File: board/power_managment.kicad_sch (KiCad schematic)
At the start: 26 parts, among them J3 Bat IN Terminal, J4 Bat OUT Terminal, Q1 PMOS, U1 INA226, U3 AMS1117-3.3, U3 INA226, U4 LM2596S-5

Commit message: More work on PCB design
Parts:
- removed C5: 100n, Capacitor_SMD:C_0201_0603Metric, symbol Device:C
- C1: footprint Diode_THT:D_DO-201_P12.70mm_Horizontal -> Capacitor_SMD:C_0603_1608Metric
- C15: footprint Capacitor_SMD:C_0603_1608Metric -> Capacitor_THT:CP_Radial_D8.0mm_P3.50mm
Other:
- moved on the sheet: C15, F1
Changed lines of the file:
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@@
     (rev "1.0")
   )
-  (junction (at 145.415 66.675) (diameter 0) (color 0 0 0 0)
-  )
   (junction (at 112.395 66.675) (diameter 0) (color 0 0 0 0)
   )
@@
   )
   (junction (at 138.43 125.095) (diameter 0) (color 0 0 0 0)
-  )
-  (junction (at 156.21 66.675) (diameter 0) (color 0 0 0 0)
   )
   (junction (at 271.145 114.935) (diameter 0) (color 0 0 0 0)
@@
     (stroke (width 0) (type default))
   )
-  (wire (pts (xy 141.605 66.675) (xy 145.415 66.675))
-    (stroke (width 0) (type default))
-  )
   (wire (pts (xy 254.635 114.935) (xy 268.605 114.935))
     (stroke (width 0) (type default))
@@
     (stroke (width 0) (type default))
   )
+  (wire (pts (xy 141.605 66.675) (xy 141.605 78.74))
+    (stroke (width 0) (type default))
+  )
   (wire (pts (xy 33.655 154.305) (xy 51.435 154.305))
     (stroke (width 0) (type default))
   )
-  (wire (pts (xy 156.21 66.675) (xy 161.925 66.675))
+  (wire (pts (xy 128.905 66.675) (xy 141.605 66.675))
     (stroke (width 0) (type default))
   )
@@
     (stroke (width 0) (type default))
   )
-  (wire (pts (xy 145.415 66.675) (xy 156.21 66.675))
-    (stroke (width 0) (type default))
-  )
   (wire (pts (xy 254.635 55.245) (xy 268.605 55.245))
     (stroke (width 0) (type default))
@@
     (stroke (width 0) (type default))
   )
-  (wire (pts (xy 145.415 66.675) (xy 145.415 78.105))
-    (stroke (width 0) (type default))
-  )
   (wire (pts (xy 271.145 100.33) (xy 271.145 104.775))
     (stroke (width 0) (type default))
   )
+  (wire (pts (xy 141.605 66.675) (xy 155.575 66.675))
+    (stroke (width 0) (type default))
+  )
   (wire (pts (xy 254.635 42.545) (xy 268.605 42.545))
     (stroke (width 0) (type default))
@@
     (stroke (width 0) (type default))
   )
-  (wire (pts (xy 156.21 85.725) (xy 156.21 97.79))
+  (wire (pts (xy 141.605 86.36) (xy 141.605 98.425))
     (stroke (width 0) (type default))
   )
@@
     (stroke (width 0) (type default))
   )
-  (wire (pts (xy 156.21 97.79) (xy 154.94 97.79))
-    (stroke (width 0) (type default))
-  )
   (wire (pts (xy 268.605 102.235) (xy 268.605 114.935))
     (stroke (width 0) (type default))
@@
     (stroke (width 0) (type default))
   )
-  (wire (pts (xy 128.905 66.675) (xy 141.605 66.675))
-    (stroke (width 0) (type default))
-  )
   (wire (pts (xy 61.595 128.905) (xy 61.595 136.525))
     (stroke (width 0) (type default))
@@
     (stroke (width 0) (type default))
   )
-  (wire (pts (xy 169.545 66.675) (xy 177.8 66.675))
+  (wire (pts (xy 163.195 66.675) (xy 171.45 66.675))
     (stroke (width 0) (type default))
   )
@@
     (stroke (width 0) (type default))
   )
-  (wire (pts (xy 156.21 66.675) (xy 156.21 78.105))
-    (stroke (width 0) (type default))
-  )
   (wire (pts (xy 29.845 129.54) (xy 29.845 128.905))
     (stroke (width 0) (type default))
@@
   )
   (wire (pts (xy 268.605 114.935) (xy 271.145 114.935))
-    (stroke (width 0) (type default))
-  )
-  (wire (pts (xy 145.415 85.725) (xy 145.415 97.79))
     (stroke (width 0) (type default))
   )
@@
     (effects (font (size 1.27 1.27)) (justify left bottom))
   )
-  (label "5V SENSE IN" (at 177.8 66.675 0) (fields_autoplaced)
+  (label "5V SENSE IN" (at 171.45 66.675 0) (fields_autoplaced)
     (effects (font (size 1.27 1.27)) (justify left bottom))
   )
@@
     )
   )
-  (symbol (lib_id "power:GND") (at 145.415 97.79 0) (unit 1)
-    (in_bom yes) (on_board yes) (dnp no) (fields_autoplaced)
-    (property "Reference" "#PWR05" (at 145.415 104.14 0)
-      (effects (font (size 1.27 1.27)) hide)
-    )
-    (property "Value" "GND" (at 145.415 102.235 0)
-      (effects (font (size 1.27 1.27)))
-    )
-    (property "Footprint" "" (at 145.415 97.79 0)
-      (effects (font (size 1.27 1.27)) hide)
-    )
-    (property "Datasheet" "" (at 145.415 97.79 0)
-      (effects (font (size 1.27 1.27)) hide)
-    )
-    (pin "1")
-    (instances
-      (project "uav_project"
-        (path "/a8bf0924-b264-4c19-8c7e-9c0e131cacba/a37df3ef-ef97-4895-80dd-f1dd3107828f"
-          (reference "#PWR05") (unit 1)
-        )
-      )
-    )
-  )
   (symbol (lib_id "Device:R") (at 51.435 149.86 0) (unit 1)
     (in_bom yes) (on_board yes) (dnp no) (fields_autoplaced)
@@
       (effects (font (size 1.27 1.27)) (justify left))
     )
-    (property "Footprint" "Diode_THT:D_DO-201_P12.70mm_Horizontal" (at 64.4652 81.915 0)
+    (property "Footprint" "Capacitor_SMD:C_0603_1608Metric" (at 64.4652 81.915 0)
       (effects (font (size 1.27 1.27)) hide)
     )
@@
         (path "/a8bf0924-b264-4c19-8c7e-9c0e131cacba/a37df3ef-ef97-4895-80dd-f1dd3107828f"
           (reference "C1") (unit 1)
-        )
-      )
-    )
-  )
-  (symbol (lib_id "Device:C") (at 145.415 81.915 0) (unit 1)
-    (in_bom yes) (on_board yes) (dnp no) (fields_autoplaced)
-    (property "Reference" "C5" (at 148.59 80.645 0)
-      (effects (font (size 1.27 1.27)) (justify left))
-    )
-    (property "Value" "100n" (at 148.59 83.185 0)
-      (effects (font (size 1.27 1.27)) (justify left))
-    )
-    (property "Footprint" "Capacitor_SMD:C_0201_0603Metric" (at 146.3802 85.725 0)
-      (effects (font (size 1.27 1.27)) hide)
-    )
-    (property "Datasheet" "~" (at 145.415 81.915 0)
-      (effects (font (size 1.27 1.27)) hide)
-    )
-    (pin "1")
-    (pin "2")
-    (instances
-      (project "uav_project"
-        (path "/a8bf0924-b264-4c19-8c7e-9c0e131cacba/a37df3ef-ef97-4895-80dd-f1dd3107828f"
-          (reference "C5") (unit 1)
         )
       )
@@
     )
   )
-  (symbol (lib_id "Device:C_Polarized") (at 156.21 81.915 0) (unit 1)
-    (in_bom yes) (on_board yes) (dnp no) (fields_autoplaced)
-    (property "Reference" "C15" (at 159.385 79.756 0)
-      (effects (font (size 1.27 1.27)) (justify left))
-    )
-    (property "Value" "100u" (at 159.385 82.296 0)
-      (effects (font (size 1.27 1.27)) (justify left))
-    )
-    (property "Footprint" "Capacitor_SMD:C_0603_1608Metric" (at 157.1752 85.725 0)
-      (effects (font (size 1.27 1.27)) hide)
-    )
-    (property "Datasheet" "~" (at 156.21 81.915 0)
+  (symbol (lib_id "Device:C_Polarized") (at 141.605 82.55 0) (unit 1)
+    (in_bom yes) (on_board yes) (dnp no) (fields_autoplaced)
+    (property "Reference" "C15" (at 144.78 80.391 0)
+      (effects (font (size 1.27 1.27)) (justify left))
+    )
+    (property "Value" "100u" (at 144.78 82.931 0)
+      (effects (font (size 1.27 1.27)) (justify left))
+    )
+    (property "Footprint" "Capacitor_THT:CP_Radial_D8.0mm_P3.50mm" (at 142.5702 86.36 0)
+      (effects (font (size 1.27 1.27)) hide)
+    )
+    (property "Datasheet" "~" (at 141.605 82.55 0)
       (effects (font (size 1.27 1.27)) hide)
     )
@@
     )
   )
-  (symbol (lib_id "power:GND") (at 154.94 97.79 0) (unit 1)
-    (in_bom yes) (on_board yes) (dnp no) (fields_autoplaced)
-    (property "Reference" "#PWR04" (at 154.94 104.14 0)
-      (effects (font (size 1.27 1.27)) hide)
-    )
-    (property "Value" "GND" (at 154.94 102.235 0)
-      (effects (font (size 1.27 1.27)))
-    )
-    (property "Footprint" "" (at 154.94 97.79 0)
-      (effects (font (size 1.27 1.27)) hide)
-    )
-    (property "Datasheet" "" (at 154.94 97.79 0)
+  (symbol (lib_id "power:GND") (at 141.605 98.425 0) (unit 1)
+    (in_bom yes) (on_board yes) (dnp no) (fields_autoplaced)
+    (property "Reference" "#PWR04" (at 141.605 104.775 0)
+      (effects (font (size 1.27 1.27)) hide)
+    )
+    (property "Value" "GND" (at 141.605 102.87 0)
+      (effects (font (size 1.27 1.27)))
+    )
+    (property "Footprint" "" (at 141.605 98.425 0)
+      (effects (font (size 1.27 1.27)) hide)
+    )
+    (property "Datasheet" "" (at 141.605 98.425 0)
       (effects (font (size 1.27 1.27)) hide)
     )
@@
     )
   )
-  (symbol (lib_id "Device:Polyfuse") (at 165.735 66.675 90) (unit 1)
+  (symbol (lib_id "Device:Polyfuse") (at 159.385 66.675 90) (unit 1)
     (in_bom yes) (on_board yes) (dnp no)
-    (property "Reference" "F1" (at 164.465 76.835 0)
-      (effects (font (size 1.27 1.27)) (justify left))
-    )
-    (property "Value" "Polyfuse" (at 166.37 76.835 0)
-      (effects (font (size 1.27 1.27)) (justify left))
-    )
-    (property "Footprint" "Fuse:Fuse_1210_3225Metric" (at 170.815 65.405 0)
+    (property "Reference" "F1" (at 158.115 76.835 0)
+      (effects (font (size 1.27 1.27)) (justify left))
+    )
+    (property "Value" "Polyfuse" (at 160.02 76.835 0)
+      (effects (font (size 1.27 1.27)) (justify left))
+    )
+    (property "Footprint" "Fuse:Fuse_1210_3225Metric" (at 164.465 65.405 0)
       (effects (font (size 1.27 1.27)) (justify left) hide)
     )
-    (property "Datasheet" "~" (at 165.735 66.675 0)
-      (effects (font (size 1.27 1.27)) hide)
-    )
+    (property "Datasheet" "~" (at 159.385 66.675 0)
+      (effects (font (size 1.27 1.27)) hide)
+    )

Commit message: First version of PCB finished
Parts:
- R2: footprint Resistor_SMD:R_1210_3225Metric -> Resistor_SMD:R_2512_6332Metric
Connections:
- net +3V3: no longer U1.2 (A0), U3.2 (A0)
- net SDA: now also U1.2 (A0)
- net SLC: now also U3.2 (A0)
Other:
- note added: "0x42"
- note added: "0x43"
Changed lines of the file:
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@@
     (effects (font (size 1.27 1.27)) (justify left top))
+  )
+  (text "0x42\n" (at 222.885 27.94 0)
+    (effects (font (size 1.8 1.8) (thickness 0.45)) (justify left bottom))
   )
   (text "Step Down (16V->5V)" (at 19.685 24.13 0)
@@
   )
   (text "INA226 BAT rail\n" (at 222.885 83.185 0)
+    (effects (font (size 1.8 1.8) (thickness 0.45)) (justify left bottom))
+  )
+  (text "0x43\n" (at 223.52 87.63 0)
     (effects (font (size 1.8 1.8) (thickness 0.45)) (justify left bottom))
   )
@@
     )
   )
+  (global_label "SDA" (shape input) (at 234.315 45.085 180) (fields_autoplaced)
+    (effects (font (size 1.27 1.27)) (justify right))
+    (property "Intersheetrefs" "${INTERSHEET_REFS}" (at 227.7617 45.085 0)
+      (effects (font (size 1.27 1.27)) (justify right) hide)
+    )
+  )
+  (global_label "SLC" (shape input) (at 234.315 104.775 180) (fields_autoplaced)
+    (effects (font (size 1.27 1.27)) (justify right))
+    (property "Intersheetrefs" "${INTERSHEET_REFS}" (at 227.8222 104.775 0)
+      (effects (font (size 1.27 1.27)) (justify right) hide)
+    )
+  )
   (global_label "SLC" (shape input) (at 234.315 52.705 180) (fields_autoplaced)
     (effects (font (size 1.27 1.27)) (justify right))
@@
     )
   )
-  (symbol (lib_id "power:+3V3") (at 234.315 45.085 90) (unit 1)
-    (in_bom yes) (on_board yes) (dnp no) (fields_autoplaced)
-    (property "Reference" "#PWR015" (at 238.125 45.085 0)
-      (effects (font (size 1.27 1.27)) hide)
-    )
-    (property "Value" "+3V3" (at 230.505 45.085 90)
-      (effects (font (size 1.27 1.27)) (justify left))
-    )
-    (property "Footprint" "" (at 234.315 45.085 0)
-      (effects (font (size 1.27 1.27)) hide)
-    )
-    (property "Datasheet" "" (at 234.315 45.085 0)
-      (effects (font (size 1.27 1.27)) hide)
-    )
-    (pin "1")
-    (instances
-      (project "uav_project"
-        (path "/a8bf0924-b264-4c19-8c7e-9c0e131cacba/a37df3ef-ef97-4895-80dd-f1dd3107828f"
-          (reference "#PWR015") (unit 1)
-        )
-      )
-    )
-  )
   (symbol (lib_id "Device:R") (at 51.435 149.86 0) (unit 1)
     (in_bom yes) (on_board yes) (dnp no) (fields_autoplaced)
@@
         (path "/a8bf0924-b264-4c19-8c7e-9c0e131cacba/a37df3ef-ef97-4895-80dd-f1dd3107828f"
           (reference "R4") (unit 1)
+        )
+      )
+    )
+  )
+  (symbol (lib_id "power:GND") (at 234.315 102.235 270) (mirror x) (unit 1)
+    (in_bom yes) (on_board yes) (dnp no) (fields_autoplaced)
+    (property "Reference" "#PWR06" (at 227.965 102.235 0)
+      (effects (font (size 1.27 1.27)) hide)
+    )
+    (property "Value" "GND" (at 231.14 102.235 90)
+      (effects (font (size 1.27 1.27)) (justify right))
+    )
+    (property "Footprint" "" (at 234.315 102.235 0)
+      (effects (font (size 1.27 1.27)) hide)
+    )
+    (property "Datasheet" "" (at 234.315 102.235 0)
+      (effects (font (size 1.27 1.27)) hide)
+    )
+    (pin "1")
+    (instances
+      (project "uav_project"
+        (path "/a8bf0924-b264-4c19-8c7e-9c0e131cacba/a37df3ef-ef97-4895-80dd-f1dd3107828f"
+          (reference "#PWR06") (unit 1)
         )
       )
@@
     )
   )
-  (symbol (lib_id "power:GND") (at 234.315 102.235 270) (unit 1)
-    (in_bom yes) (on_board yes) (dnp no) (fields_autoplaced)
-    (property "Reference" "#PWR06" (at 227.965 102.235 0)
-      (effects (font (size 1.27 1.27)) hide)
-    )
-    (property "Value" "GND" (at 230.505 102.235 90)
-      (effects (font (size 1.27 1.27)) (justify right))
-    )
-    (property "Footprint" "" (at 234.315 102.235 0)
-      (effects (font (size 1.27 1.27)) hide)
-    )
-    (property "Datasheet" "" (at 234.315 102.235 0)
-      (effects (font (size 1.27 1.27)) hide)
-    )
-    (pin "1")
-    (instances
-      (project "uav_project"
-        (path "/a8bf0924-b264-4c19-8c7e-9c0e131cacba"
-          (reference "#PWR06") (unit 1)
-        )
-        (path "/a8bf0924-b264-4c19-8c7e-9c0e131cacba/a37df3ef-ef97-4895-80dd-f1dd3107828f"
-          (reference "#PWR06") (unit 1)
-        )
-      )
-    )
-  )
-  (symbol (lib_id "power:+3V3") (at 234.315 104.775 90) (unit 1)
-    (in_bom yes) (on_board yes) (dnp no) (fields_autoplaced)
-    (property "Reference" "#PWR07" (at 238.125 104.775 0)
-      (effects (font (size 1.27 1.27)) hide)
-    )
-    (property "Value" "+3V3" (at 230.505 104.775 90)
-      (effects (font (size 1.27 1.27)) (justify left))
-    )
-    (property "Footprint" "" (at 234.315 104.775 0)
-      (effects (font (size 1.27 1.27)) hide)
-    )
-    (property "Datasheet" "" (at 234.315 104.775 0)
-      (effects (font (size 1.27 1.27)) hide)
-    )
-    (pin "1")
-    (instances
-      (project "uav_project"
-        (path "/a8bf0924-b264-4c19-8c7e-9c0e131cacba/a37df3ef-ef97-4895-80dd-f1dd3107828f"
-          (reference "#PWR07") (unit 1)
-        )
-      )
-    )
-  )
   (symbol (lib_id "power:GND") (at 33.02 39.37 90) (unit 1)
     (in_bom yes) (on_board yes) (dnp no) (fields_autoplaced)
@@
       (effects (font (size 1.27 1.27)) (justify left))
     )
-    (property "Footprint" "Resistor_SMD:R_1210_3225Metric" (at 269.367 108.585 90)
+    (property "Footprint" "Resistor_SMD:R_2512_6332Metric" (at 269.367 108.585 90)
       (effects (font (size 1.27 1.27)) hide)
     )
@@
         (path "/a8bf0924-b264-4c19-8c7e-9c0e131cacba/a37df3ef-ef97-4895-80dd-f1dd3107828f"
           (reference "#PWR010") (unit 1)
+        )
+      )
+    )
+  )
+  (symbol (lib_id "power:GND") (at 234.315 42.545 270) (mirror x) (unit 1)
+    (in_bom yes) (on_board yes) (dnp no) (fields_autoplaced)
+    (property "Reference" "#PWR09" (at 227.965 42.545 0)
+      (effects (font (size 1.27 1.27)) hide)
+    )
+    (property "Value" "GND" (at 231.14 42.545 90)
+      (effects (font (size 1.27 1.27)) (justify right))
+    )
+    (property "Footprint" "" (at 234.315 42.545 0)
+      (effects (font (size 1.27 1.27)) hide)
+    )
+    (property "Datasheet" "" (at 234.315 42.545 0)
+      (effects (font (size 1.27 1.27)) hide)
+    )
+    (pin "1")
+    (instances
+      (project "uav_project"
+        (path "/a8bf0924-b264-4c19-8c7e-9c0e131cacba/a37df3ef-ef97-4895-80dd-f1dd3107828f"
+          (reference "#PWR09") (unit 1)
         )
       )
@@
         )
       )
-    )
-  )
-  (symbol (lib_id "power:GND") (at 234.315 42.545 270) (unit 1)
-    (in_bom yes) (on_board yes) (dnp no) (fields_autoplaced)
-    (property "Reference" "#PWR06" (at 227.965 42.545 0)
-      (effects (font (size 1.27 1.27)) hide)
-    )
-    (property "Value" "GND" (at 230.505 42.545 90)
-      (effects (font (size 1.27 1.27)) (justify right))
-    )
-    (property "Footprint" "" (at 234.315 42.545 0)
-      (effects (font (size 1.27 1.27)) hide)
-    )
-    (property "Datasheet" "" (at 234.315 42.545 0)
-      (effects (font (size 1.27 1.27)) hide)
-    )
-    (pin "1")
-    (instances
-      (project "uav_project"
-        (path "/a8bf0924-b264-4c19-8c7e-9c0e131cacba"
-          (reference "#PWR06") (unit 1)
-        )
-        (path "/a8bf0924-b264-4c19-8c7e-9c0e131cacba/a37df3ef-ef97-4895-80dd-f1dd3107828f"
-          (reference "#PWR09") (unit 1)
-        )
-      )

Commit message: Minor improvements to board design
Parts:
- R1: footprint Resistor_SMD:R_1210_3225Metric -> Resistor_SMD:R_1206_3216Metric
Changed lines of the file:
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@@
       (effects (font (size 1.27 1.27)) (justify left))
     )
-    (property "Footprint" "Resistor_SMD:R_1210_3225Metric" (at 269.367 48.895 90)
+    (property "Footprint" "Resistor_SMD:R_1206_3216Metric" (at 269.367 48.895 90)
       (effects (font (size 1.27 1.27)) hide)
     )

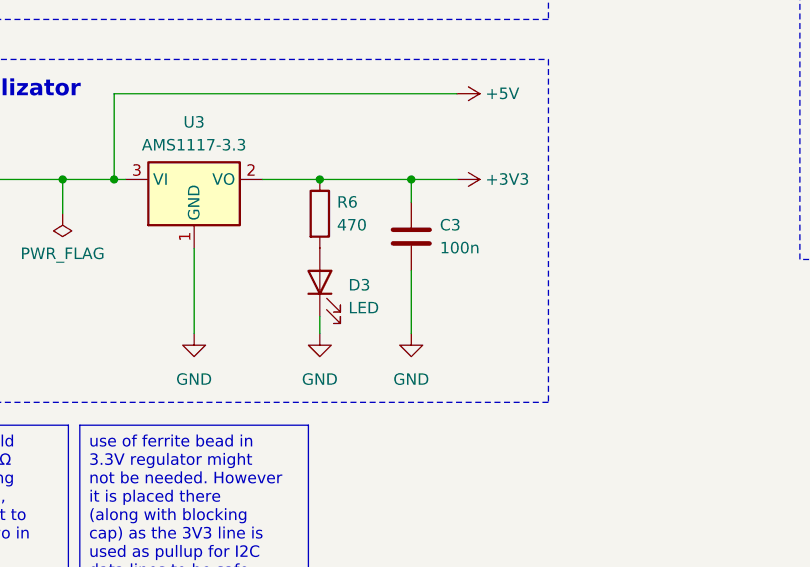
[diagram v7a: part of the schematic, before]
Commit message: Cleanup on drone side, to make code more bearable and simple
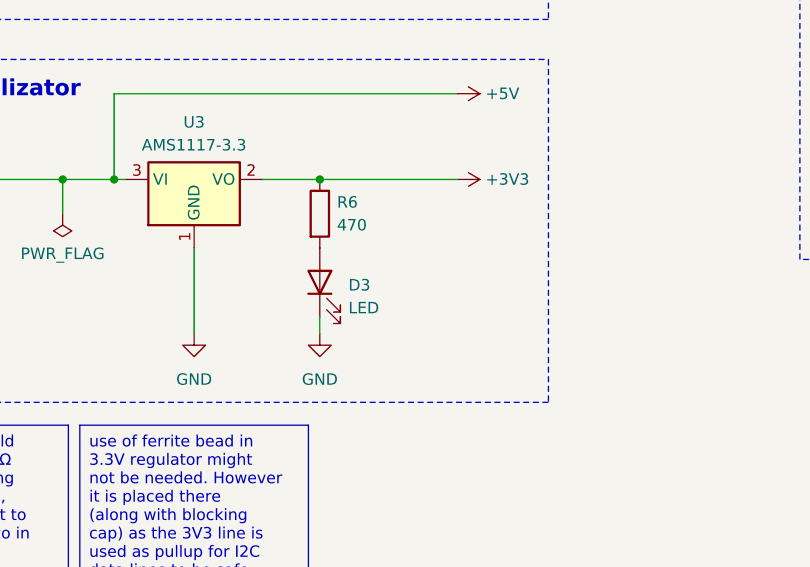
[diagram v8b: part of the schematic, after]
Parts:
- removed C3: 100n, Capacitor_SMD:C_0603_1608Metric, symbol Device:C
- L1: footprint Inductor_SMD:L_7.3x7.3_H3.5 -> Inductor_SMD:L_Bourns-SRU8043
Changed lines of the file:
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@@
   (junction (at 51.435 154.305) (diameter 0) (color 0 0 0 0)
-  )
-  (junction (at 177.165 125.095) (diameter 0) (color 0 0 0 0)
   )
   (junction (at 69.215 61.595) (diameter 0) (color 0 0 0 0)
@@
     (stroke (width 0) (type default))
   )
-  (wire (pts (xy 177.165 142.24) (xy 177.165 135.255))
-    (stroke (width 0) (type default))
-  )
   (wire (pts (xy 63.5 61.595) (xy 63.5 74.295))
     (stroke (width 0) (type default))
@@
     (stroke (width 0) (type default))
   )
-  (wire (pts (xy 177.165 125.095) (xy 182.245 125.095))
+  (wire (pts (xy 167.005 125.095) (xy 182.245 125.095))
     (stroke (width 0) (type default))
   )
@@
     (stroke (width 0) (type default))
   )
-  (wire (pts (xy 167.005 125.095) (xy 177.165 125.095))
-    (stroke (width 0) (type default))
-  )
   (wire (pts (xy 167.005 125.095) (xy 160.655 125.095))
     (stroke (width 0) (type default))
@@
   )
   (wire (pts (xy 144.145 115.57) (xy 182.245 115.57))
-    (stroke (width 0) (type default))
-  )
-  (wire (pts (xy 177.165 125.095) (xy 177.165 127.635))
     (stroke (width 0) (type default))
   )
@@
         (path "/a8bf0924-b264-4c19-8c7e-9c0e131cacba/a37df3ef-ef97-4895-80dd-f1dd3107828f"
           (reference "U4") (unit 1)
-        )
-      )
-    )
-  )
-  (symbol (lib_id "Device:C") (at 177.165 131.445 0) (unit 1)
-    (in_bom yes) (on_board yes) (dnp no) (fields_autoplaced)
-    (property "Reference" "C3" (at 180.34 130.175 0)
-      (effects (font (size 1.27 1.27)) (justify left))
-    )
-    (property "Value" "100n" (at 180.34 132.715 0)
-      (effects (font (size 1.27 1.27)) (justify left))
-    )
-    (property "Footprint" "Capacitor_SMD:C_0603_1608Metric" (at 178.1302 135.255 0)
-      (effects (font (size 1.27 1.27)) hide)
-    )
-    (property "Datasheet" "~" (at 177.165 131.445 0)
-      (effects (font (size 1.27 1.27)) hide)
-    )
-    (pin "1")
-    (pin "2")
-    (instances
-      (project "uav_project"
-        (path "/a8bf0924-b264-4c19-8c7e-9c0e131cacba/a37df3ef-ef97-4895-80dd-f1dd3107828f"
-          (reference "C3") (unit 1)
         )
       )
@@
       (effects (font (size 1.27 1.27)))
     )
-    (property "Footprint" "Inductor_SMD:L_7.3x7.3_H3.5" (at 125.095 66.675 0)
+    (property "Footprint" "Inductor_SMD:L_Bourns-SRU8043" (at 125.095 66.675 0)
       (effects (font (size 1.27 1.27)) hide)
     )
@@
         )
       )
-    )
-  )
-  (symbol (lib_id "power:GND") (at 177.165 142.24 0) (unit 1)
-    (in_bom yes) (on_board yes) (dnp no) (fields_autoplaced)
-    (property "Reference" "#PWR010" (at 177.165 148.59 0)
-      (effects (font (size 1.27 1.27)) hide)
-    )
-    (property "Value" "GND" (at 177.165 147.32 0)
-      (effects (font (size 1.27 1.27)))
-    )
-    (property "Footprint" "" (at 177.165 142.24 0)
-      (effects (font (size 1.27 1.27)) hide)
-    )
-    (property "Datasheet" "" (at 177.165 142.24 0)
-      (effects (font (size 1.27 1.27)) hide)
-    )
-    (pin "1")
-    (instances
-      (project "uav_project"
-        (path "/a8bf0924-b264-4c19-8c7e-9c0e131cacba"
-          (reference "#PWR010") (unit 1)
-        )
-        (path "/a8bf0924-b264-4c19-8c7e-9c0e131cacba/a37df3ef-ef97-4895-80dd-f1dd3107828f"
-          (reference "#PWR012") (unit 1)
-        )
-      )
